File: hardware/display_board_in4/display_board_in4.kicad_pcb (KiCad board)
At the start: 4 copper layers, 230 x 50 mm, 191 parts, among them J1 Conn_02x05_Odd_Even, J3 Conn_02x05_Odd_Even, Q1 MMBTA42, Q10 MMBTA42, Q11 MMBTA42, Q12 MMBTA42, Q13 MMBTA42, Q14 MMBTA42, Q15 MMBTA42, Q16 MMBTA42, Q17 MMBTA42, Q18 MMBTA42, Q19 MMBTA42, Q2 MMBTA42, Q20 MMBTA42, Q21 MMBTA42, Q22 MMBTA42, Q23 MMBTA42, Q24 MMBTA42, Q25 MMBTA42, Q26 MMBTA42, Q27 MMBTA42, Q28 MMBTA42, Q29 MMBTA42, Q3 MMBTA42, Q30 MMBTA42, Q31 MMBTA42, Q32 MMBTA42, Q33 MMBTA42, Q34 MMBTA42, Q35 MMBTA42, Q36 MMBTA42, Q37 MMBTA42, Q38 MMBTA42, Q39 MMBTA42, Q4 MMBTA42, Q40 MMBTA42, Q41 MMBTA42, Q42 MMBTA42, Q43 MMBTA42, Q44 MMBTA42, Q45 MMBTA42, Q46 MMBTA42, Q47 MMBTA42, Q48 MMBTA42, Q49 MMBTA42, Q5 MMBTA42, Q50 MMBTA42, Q51 MMBTA42, Q52 MMBTA42, Q53 MMBTA42, Q54 MMBTA42, Q55 MMBTA42, Q56 MMBTA42, Q57 MMBTA42, Q58 MMBTA42, Q59 MMBTA42, Q6 MMBTA42, Q60 MMBTA42, Q7 MMBTA42, Q8 MMBTA42, Q9 MMBTA42, U1 PCA9685PW, U2 PCA9685PW, U3 PCA9685PW, U4 PCA9685PW, U5 LTR-303ALS-01

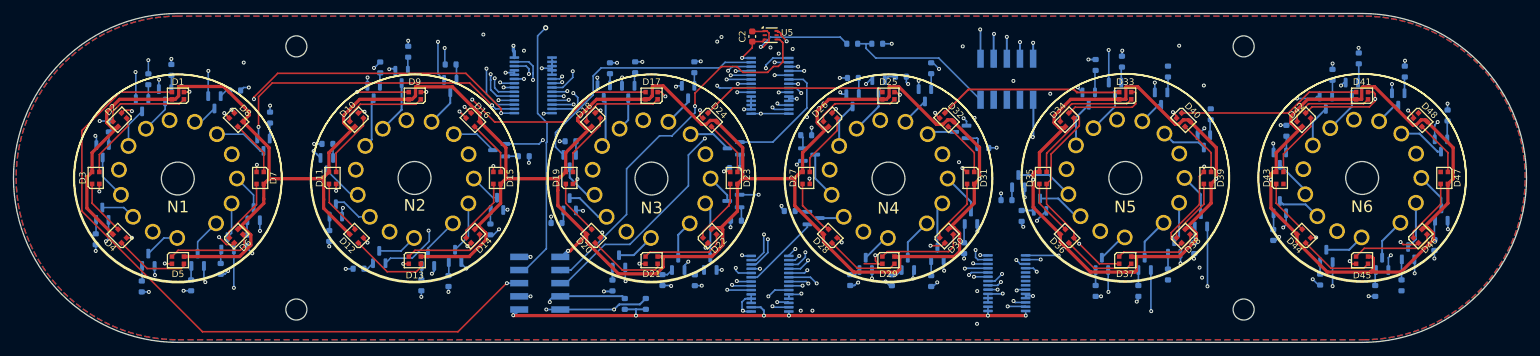
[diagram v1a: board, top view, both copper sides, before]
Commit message: fix(hw): update display board layout
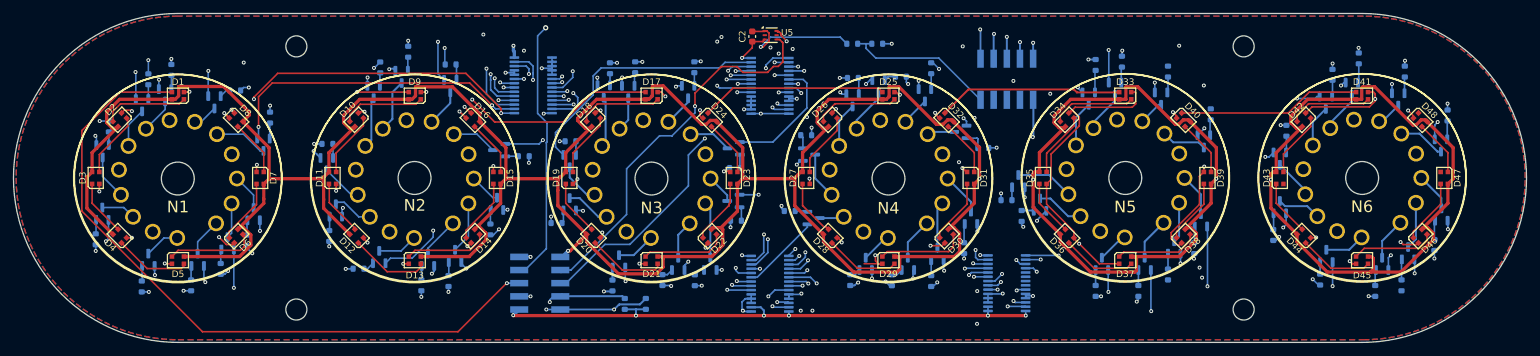
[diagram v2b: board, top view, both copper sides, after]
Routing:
- net /N3_B5: track 45.1 -> 46.8 mm
- net /N6_B3: track 71.1 -> 69.8 mm
- net /N2_B8: track 45.6 -> 46.8 mm
- net ANODE3: track 71.2 -> 70.3 mm
- net /N4_B8: track 40.8 -> 40.2 mm
